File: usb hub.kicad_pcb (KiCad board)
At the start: 2 copper layers, 65 x 30.4 mm, 22 parts, among them J1 TYPE_C, U1 FE1.1s

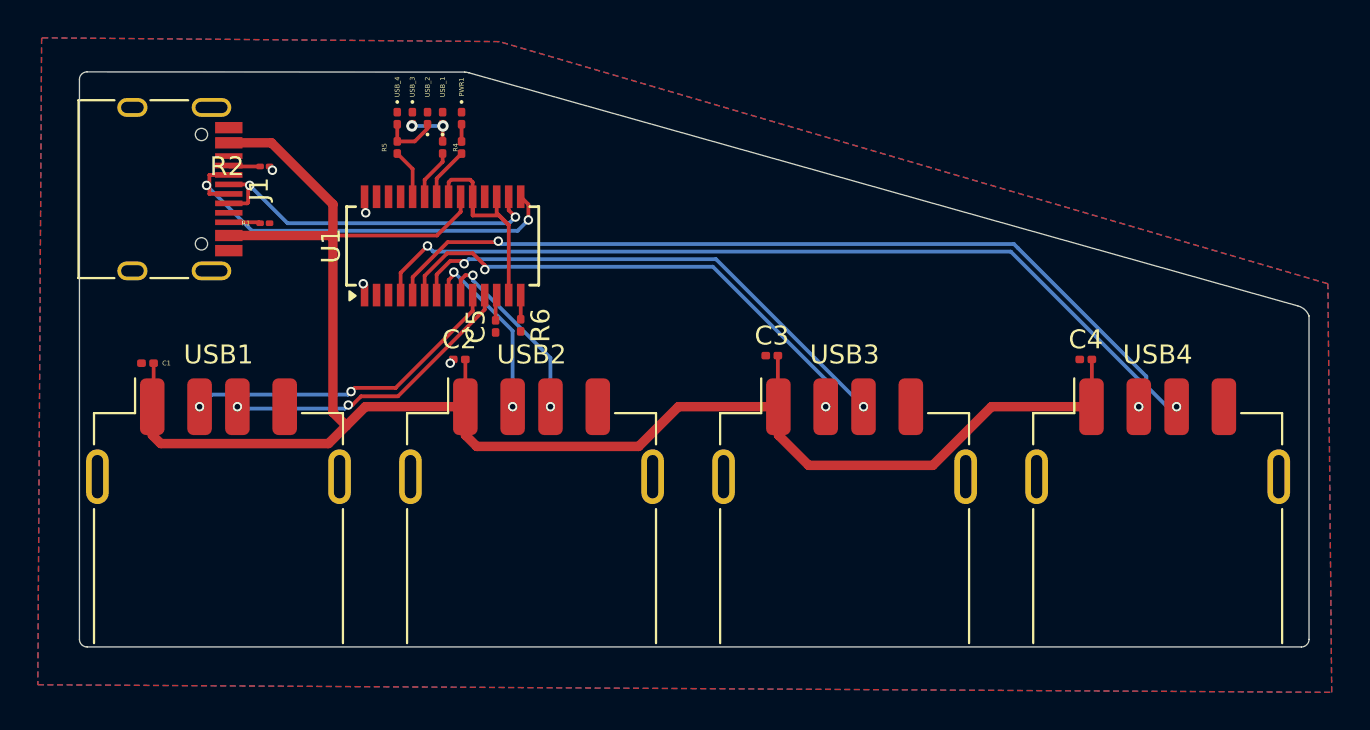
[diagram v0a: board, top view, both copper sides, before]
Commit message: fixed some sch stuff, need to add holes still
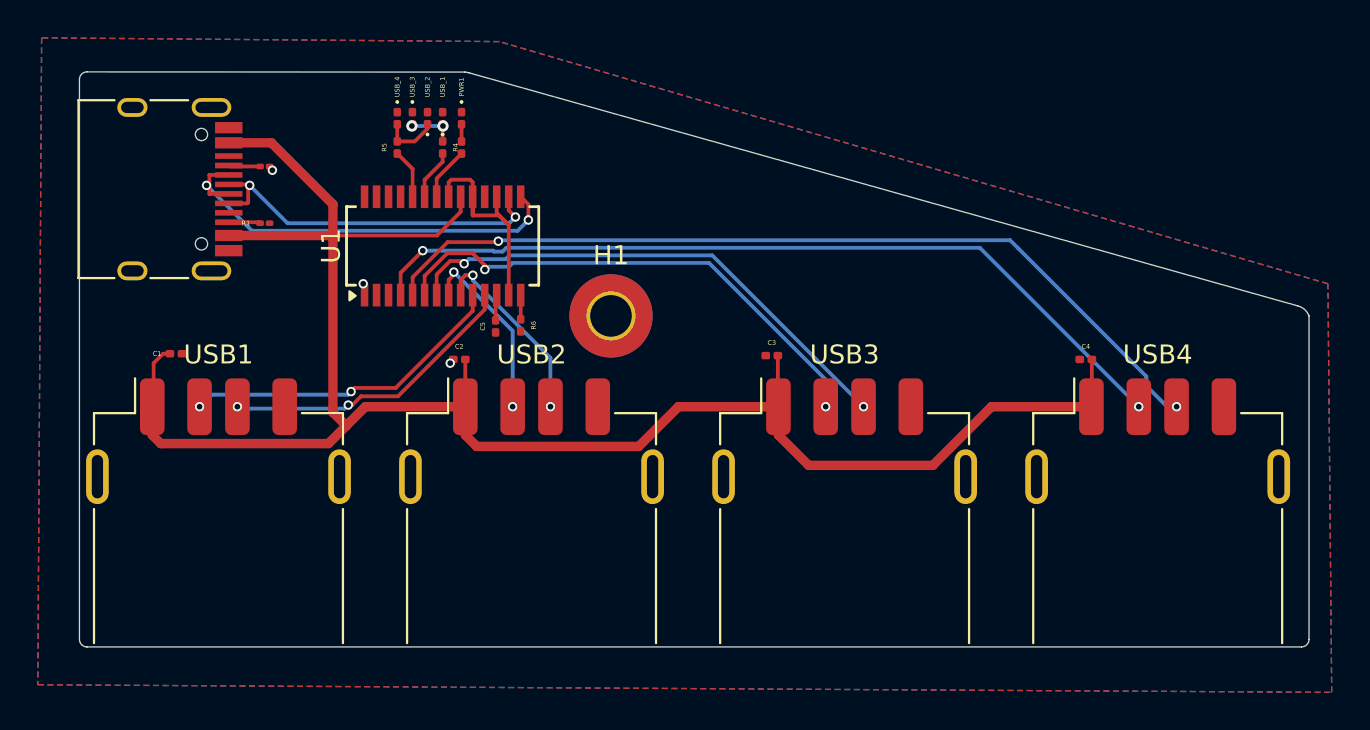
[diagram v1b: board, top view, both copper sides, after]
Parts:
- added G***: LOGO, LOGO, B.Cu at (140.0, 100.0)
- added H1: MountingHole_Pad, MountingHole:MountingHole_2.2mm_M2_Pad_TopBottom, F.Cu at (145.5, 98.5)
- moved C1 1.58 mm to (122.5, 100.5), turned to 180 degrees
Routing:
- net +5V: track 101.2 -> 102.3 mm
- net D4_N: track 45.2 -> 44.3 mm
- net unconnected-(U1-VD18-Pad28): track 0.88 -> 0.02 mm, vias 1 -> 0
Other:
- board text added: "Created by blazecoding.xyz HackClub OnBoard USB HUB V2"
